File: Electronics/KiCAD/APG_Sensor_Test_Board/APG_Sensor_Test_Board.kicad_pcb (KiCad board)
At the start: 2 copper layers, 100 x 100 mm, 85 parts, among them J1 Conn_01x02, J2 Conn_01x05, J3 Conn_01x02, J4 USB_C_Receptacle_USB2.0_16P, SW1 SW_SPST, SW2 SW_SPST, SW3 SW_SPST, SW4 SW_SPST, U1 ESP32-S3-WROOM-1, U2 BNO085, U3 ADXL375, U4 MS5607-02BA, U5 W25Q128JVS, U6 TLV1117-33

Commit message: Layout and routing
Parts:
- removed TP6: IMU_BOOT, TestPoint:TestPoint_Pad_3.0x3.0mm
- added C14: 1u, Capacitor_SMD:C_0603_1608Metric, F.Cu at (112.5, 75.3)
- added D4: SS12, Diode_SMD:D_SMA, F.Cu at (109.3, 78.9)
- added H1: MountingHole, MountingHole:MountingHole_3.2mm_M3, F.Cu at (100.8, 54.0)
- added H2: MountingHole, MountingHole:MountingHole_3.2mm_M3, F.Cu at (192.9, 54.0)
- added H3: MountingHole, MountingHole:MountingHole_3.2mm_M3, F.Cu at (100.8, 86.8)
- added H4: MountingHole, MountingHole:MountingHole_3.2mm_M3, F.Cu at (192.9, 86.8)
- added R29: 10k, Resistor_SMD:R_0603_1608Metric, F.Cu at (156.9, 74.1)
- added R30: 10k, Resistor_SMD:R_0603_1608Metric, F.Cu at (144.7, 82.7)
- added R31: 10k, Resistor_SMD:R_0603_1608Metric, F.Cu at (166.0, 52.8)
- added U7: TLV75533PDBV, Package_TO_SOT_SMD:SOT-23-5, F.Cu at (110.3, 83.2)
- C1, C10, C11, C12, C13, C2, C3, C4, C5, C6, C7, C8, C9: footprint Capacitor_SMD:C_0805_2012Metric -> Capacitor_SMD:C_0603_1608Metric
- C15: renamed from C14; footprint Capacitor_SMD:C_0805_2012Metric -> Capacitor_SMD:C_0603_1608Metric
- C16: renamed from C15; footprint Capacitor_SMD:C_0805_2012Metric -> Capacitor_SMD:C_0603_1608Metric
- C17: renamed from C16; footprint Capacitor_SMD:C_0805_2012Metric -> Capacitor_SMD:C_0603_1608Metric
- G***: moved to B.Cu
- J2: value Conn_01x05 -> Conn_01x06; footprint Connector_PinHeader_2.54mm:PinHeader_1x05_P2.54mm_Vertical -> Connector_PinHeader_2.54mm:PinHeader_1x06_P2.54mm_Vertical
- R1, R10, R11, R12, R13, R14, R15, R16, R17, R18, R19, R2, R20, R21, R22, R23, R24, R25, R26, R27, R28, R3, R4, R5, R6, R7, R8, R9: footprint Resistor_SMD:R_0805_2012Metric -> Resistor_SMD:R_0603_1608Metric
- TP1, TP10, TP11, TP12, TP13, TP14, TP15, TP16, TP17, TP18, TP19, TP2, TP3, TP4, TP5, TP7, TP8, TP9: footprint TestPoint:TestPoint_Pad_3.0x3.0mm -> TestPoint:TestPoint_Pad_D1.0mm; moved to B.Cu
- TP20, TP21: footprint TestPoint:TestPoint_Pad_3.0x3.0mm -> TestPoint:TestPoint_Pad_D1.0mm
- U6: value TLV1117-33 -> TPCM1293A-04SO; footprint Package_TO_SOT_SMD:SOT-223-3_TabPin2 -> Package_TO_SOT_SMD:SOT-23-6
- moved SW1 144.7 mm to (171.0, 51.5)
- moved SW2 142.8 mm to (180.7, 51.5)
- moved TP12 140.5 mm to (161.5, 52.8), turned to 180 degrees
- moved TP14 140.5 mm to (162.1, 64.2), turned to 180 degrees
- moved TP5 138.0 mm to (149.9, 70.5), turned to 180 degrees
- moved TP3 137.3 mm to (153.7, 70.8), turned to 180 degrees
- moved TP1 136.2 mm to (156.1, 71.0), turned to 180 degrees
- moved R10 135.1 mm to (186.4, 58.6), turned to 180 degrees
- moved C2 134.9 mm to (181.8, 58.6), turned to 180 degrees
- moved TP18 134.8 mm to (168.5, 77.2), turned to 180 degrees
- moved TP19 134.5 mm to (166.3, 77.1), turned to 180 degrees
- moved TP4 133.8 mm to (149.4, 74.6), turned to 180 degrees
- moved TP17 132.7 mm to (161.4, 60.1), turned to 180 degrees
- moved TP16 131.3 mm to (159.8, 54.9), turned to 180 degrees
- moved TP7 130.9 mm to (157.1, 81.0), turned to 180 degrees
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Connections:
- C16 pad 1: +5V -> Net-(D4-K)
- J2 pad 1: /ESP32/IO18 -> /ESP32/IO8
- J2 pad 2: /ESP32/IO39 -> /ESP32/IO18
- J2 pad 3: /ESP32/IO40 -> /ESP32/IO39
- J2 pad 4: /ESP32/IO41 -> /ESP32/IO40
- J2 pad 5: /ESP32/IO42 -> /ESP32/IO41
- R12 pad 2: /IMU_BOOT -> Net-(U2-BOOTN)
- R3 pad 2: /ESP32/IO1 -> /ESP32/IO36
- R4 pad 2: /ESP32/IO2 -> /ESP32/IO35
- R5 pad 1: /ESP32/IO1 -> /ESP32/IO36
- R6 pad 1: /ESP32/IO2 -> /ESP32/IO35
- R7 pad 1: /Baro/BARO_SDA -> /Baro/BARO_CLK
- R8 pad 1: /Baro/BARO_CLK -> /Baro/BARO_SDA
- TP12 pad 1: /ESP32/IO38 -> /ESP32/IO1
- TP16 pad 1: /ESP32/IO36 -> /ESP32/IO2
- TP17 pad 1: /ESP32/IO35 -> /ESP32/IO38
- U1 pad 10: /Debug/Button 2 -> /Debug/Buzzer
- U1 pad 12: /HIGH_G_INT2 -> /ESP32/IO8
- U1 pad 15: /HIGH_G_INT1 -> /HIGH_G_INT2
- U1 pad 17: /SCS_HIGH_G -> /HIGH_G_INT1
- U1 pad 18: /IMU_RST -> /SCS_HIGH_G
- U1 pad 19: /IMU_PS0/WAKE -> /IMU_RST
- U1 pad 20: /IMU_BOOT -> /IMU_PS0/WAKE
- U1 pad 22: /SCS_IMU -> /SMISO
- U1 pad 25: /SMISO -> /SCS_IMU
- U1 pad 5: /Debug/Debug 1 -> /Debug/Button 2
- U1 pad 6: /Debug/Debug 2 -> /Debug/Button 1
- U1 pad 7: /Debug/Debug 3 -> /Debug/Debug 1
- U1 pad 8: /Debug/Buzzer -> /Debug/Debug 2
- U1 pad 9: /Debug/Button 1 -> /Debug/Debug 3
- U2 pad 4: /IMU_BOOT -> Net-(U2-BOOTN)
- U5 pad 1: /ESP32/IO38 -> /ESP32/IO1
- U5 pad 2: /ESP32/IO36 -> /ESP32/IO2
- U5 pad 5: /ESP32/IO35 -> /ESP32/IO38
- U6 pad 1: GND -> /ESP32/USB_D_P
- U6 pad 2: +3V3 -> GND
- U6 pad 3: +5V -> /ESP32/USB_D_N
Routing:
- net /ESP32/IO8: track 0.00 -> 60.4 mm, vias 0 -> 1
- net /ESP32/IO18: track 0.00 -> 59.9 mm, vias 0 -> 1
- net /ESP32/IO0: track 0.00 -> 58.0 mm, vias 0 -> 1
- net /ESP32/ESP_EN: track 0.00 -> 47.8 mm, vias 0 -> 1
- net /ESP32/IO39: track 0.00 -> 43.3 mm, vias 0 -> 1
- net /ESP32/IO40: track 0.00 -> 41.9 mm, vias 0 -> 1
- net /ESP32/USB_D_P: track 3.50 -> 45.3 mm, vias 0 -> 1
- net /ESP32/IO41: track 0.00 -> 41.6 mm, vias 0 -> 1
- net /Debug/Button 2: track 0.00 -> 41.4 mm
- net /ESP32/IO42: track 0.00 -> 40.8 mm, vias 0 -> 1
- net /ESP32/RX: track 0.00 -> 39.7 mm, vias 0 -> 1
- net /ESP32/TX: track 0.00 -> 39.2 mm, vias 0 -> 1
- net /ESP32/USB_D_N: track 4.31 -> 42.0 mm, vias 0 -> 1
- net /Debug/Debug 3: track 0.00 -> 37.2 mm
- net /Debug/Debug 2: track 0.00 -> 36.6 mm
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- added copper zone on In2.Cu, net +3V3
- added copper zone on In1.Cu, net GND
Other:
- board size 100 x 100 mm -> 100 x 40.6 mm
- copper layers 2 -> 4
- board text added: "+3.3V"
- board text added: "+5V"
- board text added: "BARO_CLK"
- board text added: "BARO_SDA"
- board text added: "D+"
- board text added: "D-"
- board text added: "DB1"
- board text added: "DB2"
- board text added: "DB3"
- board text added: "ESP_EN"
- board text added: "FCLK"
- board text added: "FCS"
- board text added: "FMISO"
- board text added: "FMOSI"
- board text added: "GND"
- board text added: "HIGH_G_CS"
- board text added: "HIGH_G_INT1"
- board text added: "HIGH_G_INT2"
- board text added: "IMU_CS"
- board text added: "IMU_INT"
- board text added: "IMU_RST"
- board text added: "IMU_WAKE"
- board text added: "IO0"
- board text added: "SCLK"
- board text added: "SMISO"
- board text added: "SMOSI"
- board text added: "SW1"
- board text added: "SW2"

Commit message: layout changes
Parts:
- removed TP13: D_P, TestPoint:TestPoint_Pad_D1.0mm
- removed TP15: D_N, TestPoint:TestPoint_Pad_D1.0mm
- moved TP20 25.7 mm to (131.9, 81.4), turned to 90 degrees
- moved J4 25.5 mm to (121.8, 87.0), turned to 0 degrees
- moved BZ1 25.1 mm to (103.6, 74.0), turned to 0 degrees
- moved U7 22.6 mm to (132.2, 77.2), turned to 0 degrees
- moved C17 22.1 mm to (133.3, 73.5), turned to 90 degrees
- moved TP21 19.6 mm to (131.4, 73.8), turned to 90 degrees
- moved D4 18.7 mm to (128.0, 78.3), turned to -90 degrees
- moved FB1 17.8 mm to (124.4, 80.3), turned to 0 degrees
- moved C16 16.2 mm to (128.9, 73.6), turned to 0 degrees
- moved C15 15.3 mm to (124.4, 78.2), turned to 180 degrees
- moved R28 14.4 mm to (114.0, 85.2), turned to 180 degrees
- moved R27 13.3 mm to (114.0, 87.2), turned to 180 degrees
- moved C14 11.8 mm to (124.4, 75.0), turned to 180 degrees
- moved U6 10.3 mm to (120.1, 76.3), turned to 0 degrees
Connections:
- U7 pad 2: unconnected-(U7-GND-Pad2) -> GND
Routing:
- net /ESP32/USB_D_P: track 45.3 -> 32.2 mm, vias 1 -> 0
- net /ESP32/USB_D_N: track 42.0 -> 30.2 mm, vias 1 -> 0
- net Net-(BZ1-+): track 12.1 -> 2.11 mm
- net GND: track 31.5 -> 38.7 mm, vias 26 -> 30
- net Net-(J4-CC1): track 11.7 -> 7.51 mm
- net Net-(J4-CC2): track 8.14 -> 11.8 mm
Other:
- board text removed: "D+"
- board text removed: "D-"

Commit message: new tvs diode debug changes
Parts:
- added C14: 0.1uF, Capacitor_SMD:C_0603_1608Metric, F.Cu at (122.2, 76.5)
- U6: value TPCM1293A-04SO -> USBULC6-2M6; footprint Package_TO_SOT_SMD:SOT-23-6 -> Package_DFN_QFN:ST_UQFN-6L_1.5x1.7mm_P0.5mm
- moved TP20 21.6 mm to (110.5, 78.5)
- moved U7 15.2 mm to (117.2, 74.8)
- moved D4 14.8 mm to (113.2, 76.5)
- moved C17 14.3 mm to (119.2, 72.0), turned to 0 degrees
- moved C16 13.7 mm to (115.3, 72.0), turned to 180 degrees
- moved TP21 13.6 mm to (118.4, 70.0), turned to 0 degrees
- moved C14 11.8 mm to (114.0, 80.8)
- moved C15 11.1 mm to (114.0, 82.2)
- moved FB1 7.18 mm to (117.2, 80.8), turned to 180 degrees
- moved R19 5.83 mm to (166.5, 88.2), turned to 90 degrees
- moved U6 3.61 mm to (122.2, 79.2), turned to 90 degrees
- moved C10 3.00 mm to (167.3, 85.9)
- moved R17 3.00 mm to (169.7, 86.7)
- moved R18 3.00 mm to (171.3, 86.7)
- moved U4 3.00 mm to (168.4, 83.1)
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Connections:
- U6 pad 1: /ESP32/USB_D_P -> /ESP32/USB_D_N
- U6 pad 3: /ESP32/USB_D_N -> /ESP32/USB_D_P
- U6 pad 4: unconnected-(U6-CH3-Pad4) -> /ESP32/USB_D_P
- U6 pad 5: +5V -> Net-(U6-CAP)
- U6 pad 6: unconnected-(U6-CH4-Pad6) -> /ESP32/USB_D_N
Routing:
- net Net-(BZ1-+): track 2.11 -> 32.5 mm
- net +5V: track 16.8 -> 9.43 mm
- net /ESP32/USB_D_N: track 30.2 -> 37.3 mm
- net /ESP32/USB_D_P: track 32.2 -> 37.5 mm
- net /Baro/BARO_SDA: track 6.24 -> 9.44 mm
- net /Baro/BARO_CLK: track 5.74 -> 8.95 mm
- net Net-(D4-K): track 8.88 -> 7.15 mm
- net Net-(U6-CAP): track 0.00 -> 1.32 mm
- net +3V3: track 8.02 -> 8.89 mm
- net GND: track 38.7 -> 38.0 mm, vias 30 -> 29
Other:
- outline, holes or cut-outs redrawn

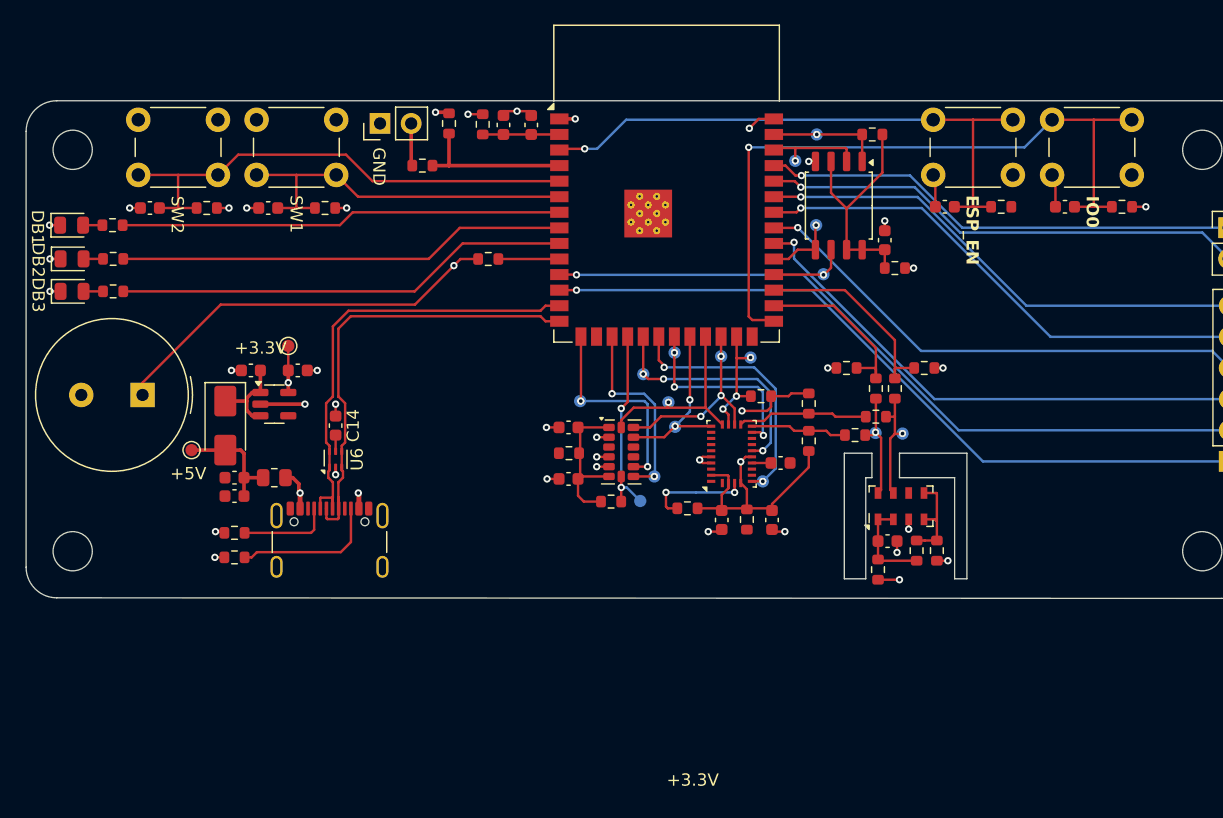
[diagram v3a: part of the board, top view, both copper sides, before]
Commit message: Edit PCB and Update component values
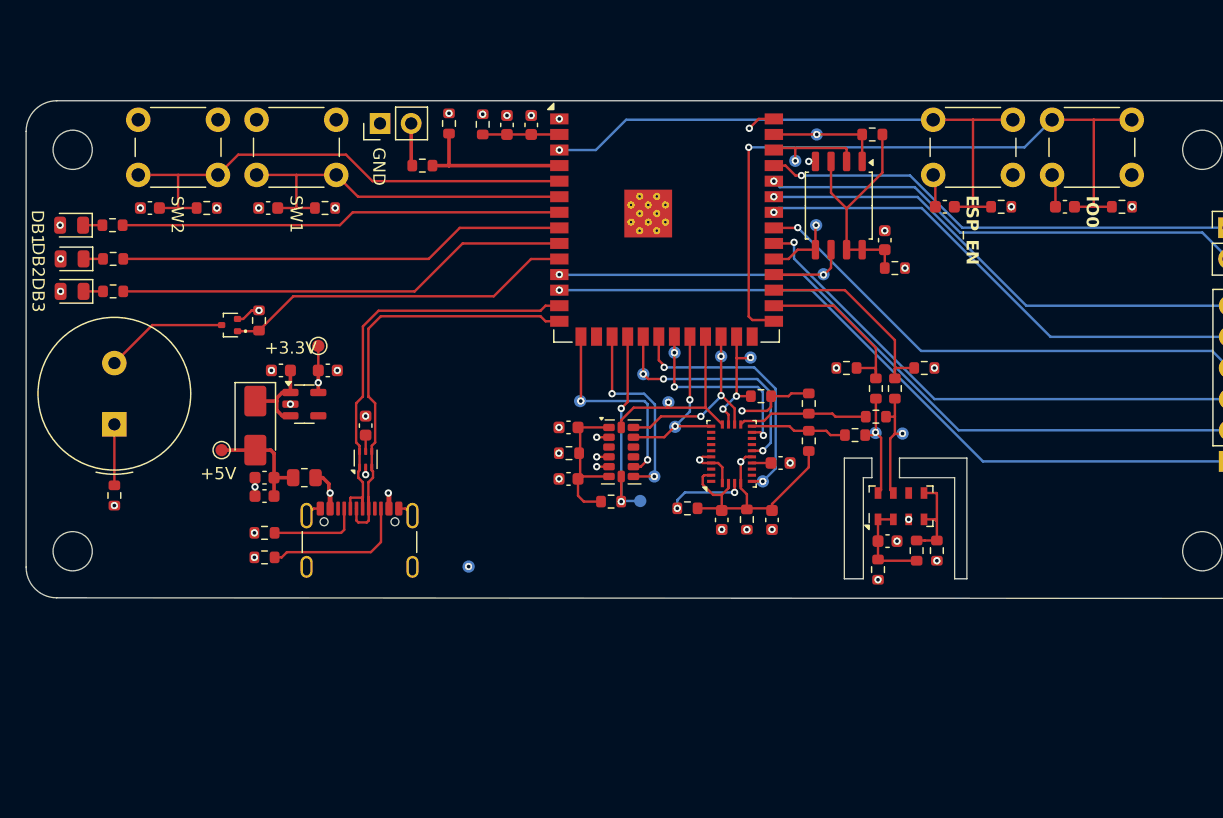
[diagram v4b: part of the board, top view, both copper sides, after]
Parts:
- added Q1: RE1C002UNTCL, Package_TO_SOT_SMD:SOT-416, F.Cu at (113.6, 68.3)
- added R32: 10k, Resistor_SMD:R_0603_1608Metric, F.Cu at (116.0, 67.9)
- added TP6: SCS_IMU, TestPoint:TestPoint_Pad_D1.0mm, B.Cu at (133.1, 88.0)
- C5: value 0.1uF -> 1uf
- R22: value 200 -> 65
- R23: value 200 -> 25
- R24: value 200 -> 52
- moved R21 36.1 mm to (104.2, 82.2), turned to 90 degrees
- moved BZ1 3.32 mm to (104.2, 76.4), turned to 90 degrees
- moved C14 2.45 mm to (124.7, 76.5)
- moved C14 2.45 mm to (116.5, 80.8)
- moved C15 2.45 mm to (116.5, 82.2)
- moved C17 2.45 mm to (121.6, 72.0)
- moved D4 2.45 mm to (115.7, 76.5)
- moved FB1 2.45 mm to (119.7, 80.8)
- moved J4 2.45 mm to (124.2, 87.0)
- moved R27 2.45 mm to (116.5, 87.2)
- moved R28 2.45 mm to (116.5, 85.2)
- moved TP20 2.45 mm to (113.0, 78.5)
- moved TP21 2.45 mm to (120.8, 70.0)
- moved U6 2.45 mm to (124.7, 79.2)
- moved U7 2.45 mm to (119.7, 74.8)
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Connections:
- BZ1 pad 2: GND -> Net-(BZ1--)
- D1 pad 1: GND -> Net-(D1-K)
- D1 pad 2: Net-(D1-A) -> +3V3
- D2 pad 1: GND -> Net-(D2-K)
- D2 pad 2: Net-(D2-A) -> +3V3
- D3 pad 1: GND -> Net-(D3-K)
- D3 pad 2: Net-(D3-A) -> +3V3
- R10 pad 1: +3.3V -> +3V3
- R21 pad 1: /Debug/Buzzer -> +3V3
- R22 pad 2: Net-(D1-A) -> Net-(D1-K)
- R23 pad 2: Net-(D2-A) -> Net-(D2-K)
- R24 pad 2: Net-(D3-A) -> Net-(D3-K)
- R25 pad 1: +3.3V -> +3V3
- R26 pad 1: +3.3V -> +3V3
- R9 pad 1: +3.3V -> +3V3
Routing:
- net Net-(BZ1-+): track 32.5 -> 4.97 mm, vias 1 -> 0
- net /Debug/Buzzer: track 4.89 -> 28.7 mm
- net GND: track 38.0 -> 23.8 mm, vias 29 -> 31
- net Net-(BZ1--): track 0.00 -> 10.1 mm
- net +3V3: track 8.89 -> 3.80 mm, vias 6 -> 16
- net +3.3V: track 3.05 -> 0.00 mm, vias 3 -> 0
- net /ESP32/USB_D_N: track 37.3 -> 34.9 mm
- net /ESP32/USB_D_P: track 37.5 -> 35.5 mm
- net Net-(U2-BOOTN): track 8.41 -> 6.46 mm
- net Net-(D3-K): track 0.00 -> 1.94 mm
- net Net-(D3-A): track 1.94 -> 0.00 mm
- net Net-(D2-K): track 0.00 -> 1.94 mm
- net Net-(D2-A): track 1.94 -> 0.00 mm
- net Net-(D1-K): track 0.00 -> 1.92 mm
- net Net-(D1-A): track 1.92 -> 0.00 mm
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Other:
- outline, holes or cut-outs redrawn

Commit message: APG Sensor Board V1.1 Production
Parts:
- moved G*** 4.73 mm to (180.2, 68.2)
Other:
- board text added: "APG_Sensor_Board_V1.1 Gannon Bird Ethan Benne Nathan Emerson Tannyr Singleterry"
